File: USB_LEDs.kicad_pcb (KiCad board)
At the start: 2 copper layers, 100 x 20 mm, 35 parts, among them U1 MT9284, U2 JL8022W-L

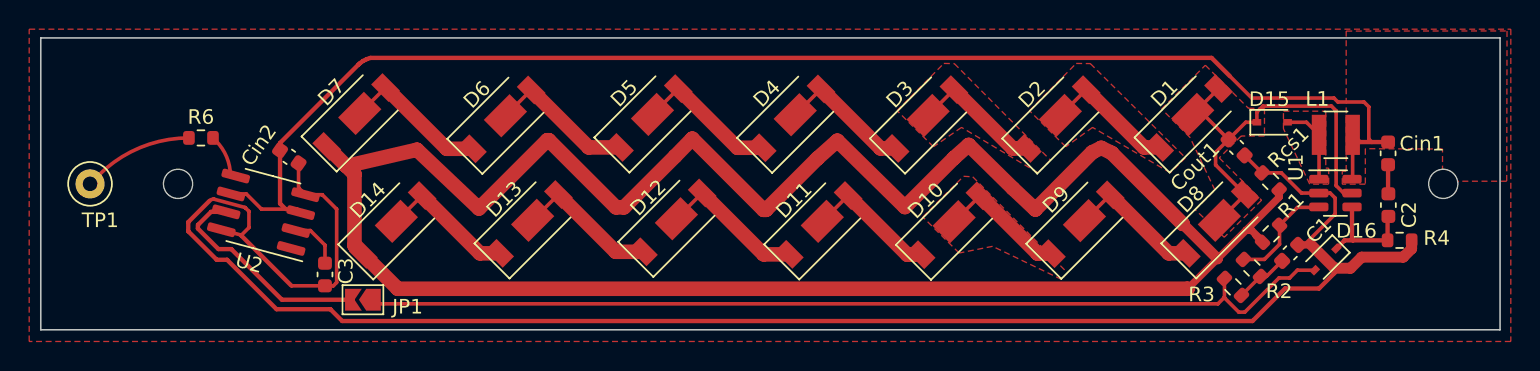
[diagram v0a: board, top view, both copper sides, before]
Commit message: Added copper pours surrounding the LED pads
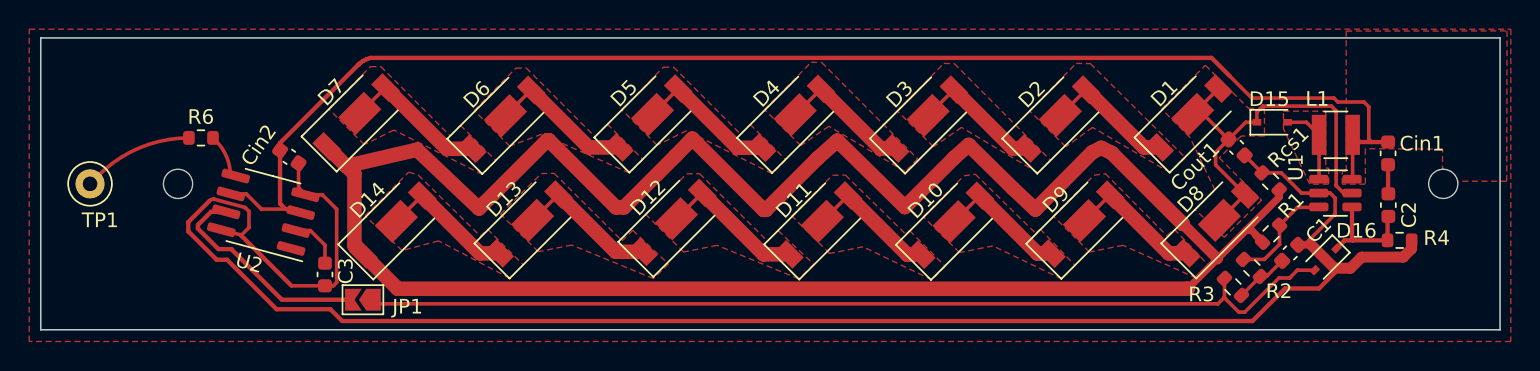
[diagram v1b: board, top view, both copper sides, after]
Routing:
- added copper zone on F.Cu, net Net-(D10-Pad1)
- added copper zone on F.Cu, net Net-(D11-Pad1)
- added copper zone on F.Cu, net Net-(D12-Pad1)
- added copper zone on F.Cu, net Net-(D13-Pad1)
- added copper zone on F.Cu, net Net-(D3-Pad1)
- added copper zone on F.Cu, net Net-(D4-Pad1)
- added copper zone on F.Cu, net Net-(D5-Pad1)
- added copper zone on F.Cu, net Net-(D6-Pad1)
- added copper zone on F.Cu, net Net-(D8-Pad1)

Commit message: Squeezed tracks and components closer
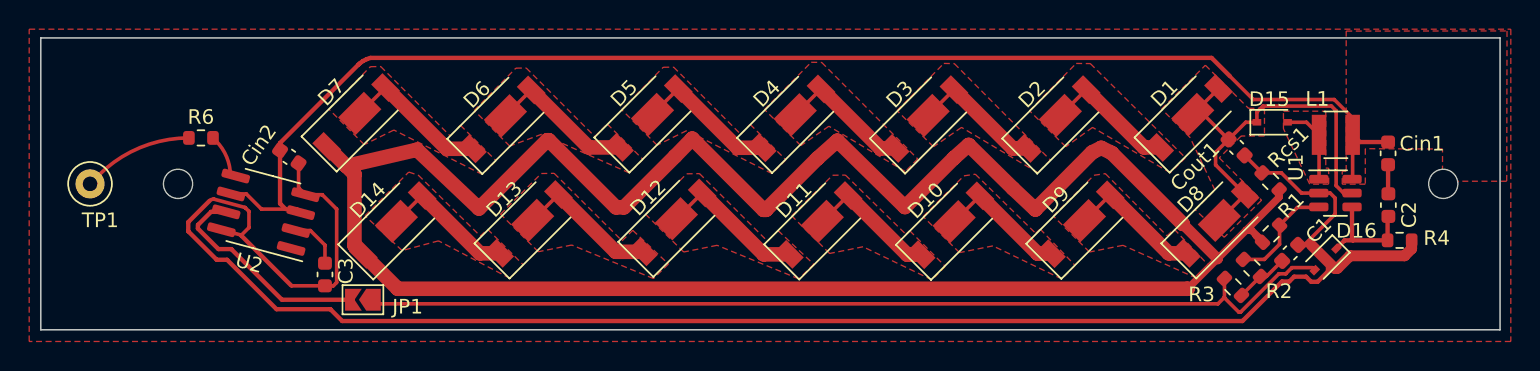
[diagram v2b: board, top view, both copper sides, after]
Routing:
- net +5V: track 96.5 -> 94.4 mm
- net GND: track 133.4 -> 135.2 mm

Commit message: Added an inverter to correct the dimming feature
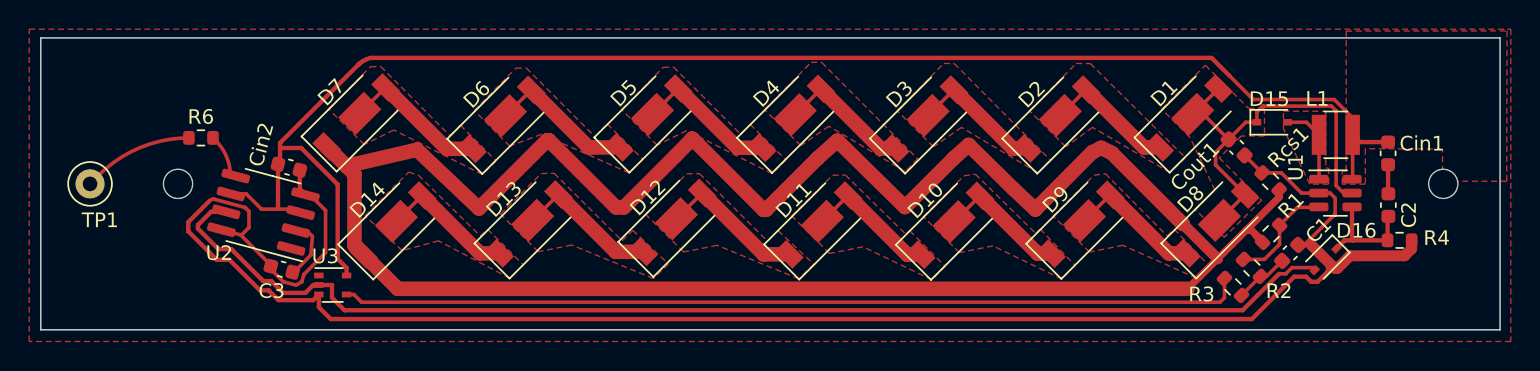
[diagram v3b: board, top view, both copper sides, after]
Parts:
- removed JP1: SolderJumper_2_Open, Jumper:SolderJumper-2_P1.3mm_Open_TrianglePad1.0x1.5mm
- added U3: 74LVC1G04, Package_TO_SOT_SMD:SOT-353_SC-70-5, F.Cu at (38.0, 36.1)
- moved C3 2.98 mm to (34.6, 35.0), turned to 165 degrees
- moved Cin2 0.72 mm to (35.0, 28.0), turned to 165 degrees
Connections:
- R3 pad 1: Net-(D16-Pad2) -> Net-(U3-Pad4)
- U2 pad 7: DIM -> Net-(D16-Pad2)
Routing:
- net Net-(U3-Pad4): track 0.00 -> 61.8 mm
- net Net-(D16-Pad2): track 67.9 -> 83.6 mm
- net DIM: track 15.1 -> 0.00 mm
- net +5V: track 94.4 -> 105.7 mm
- net GND: track 135.2 -> 132.7 mm
- net Net-(C3-Pad1): track 3.64 -> 4.31 mm
